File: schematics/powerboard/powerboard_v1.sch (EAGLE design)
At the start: 38 parts, among them IC1 ACS756LCB-100B-PFF-T, IC2 ATMEGA644-A, Y1 10MHZ

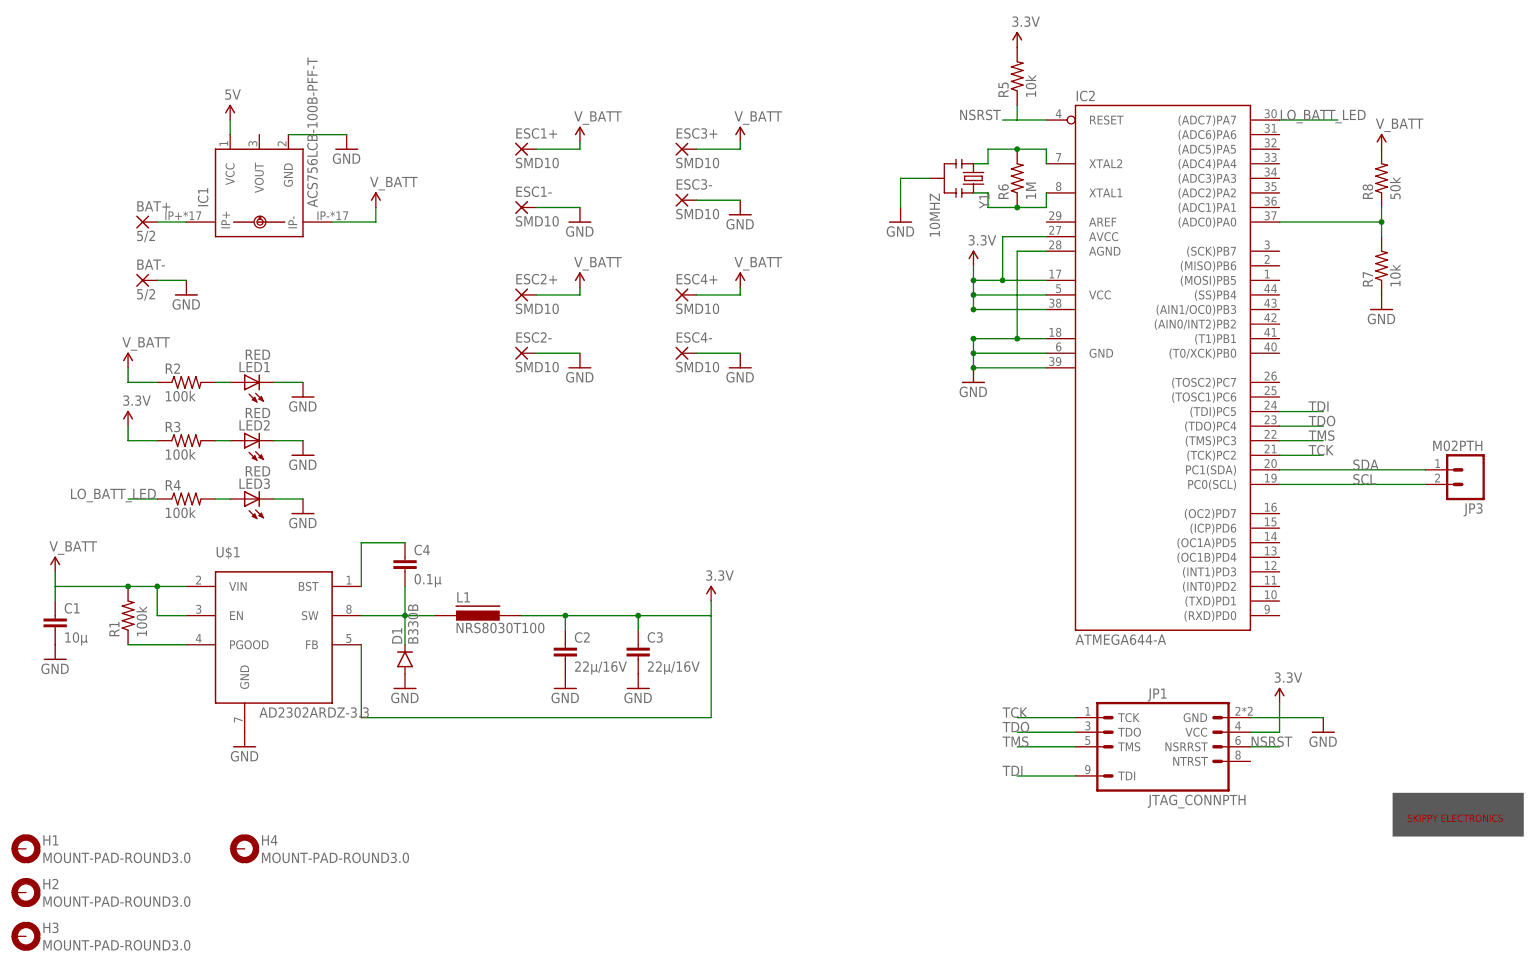
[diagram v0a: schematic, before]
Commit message: New PCB for power board
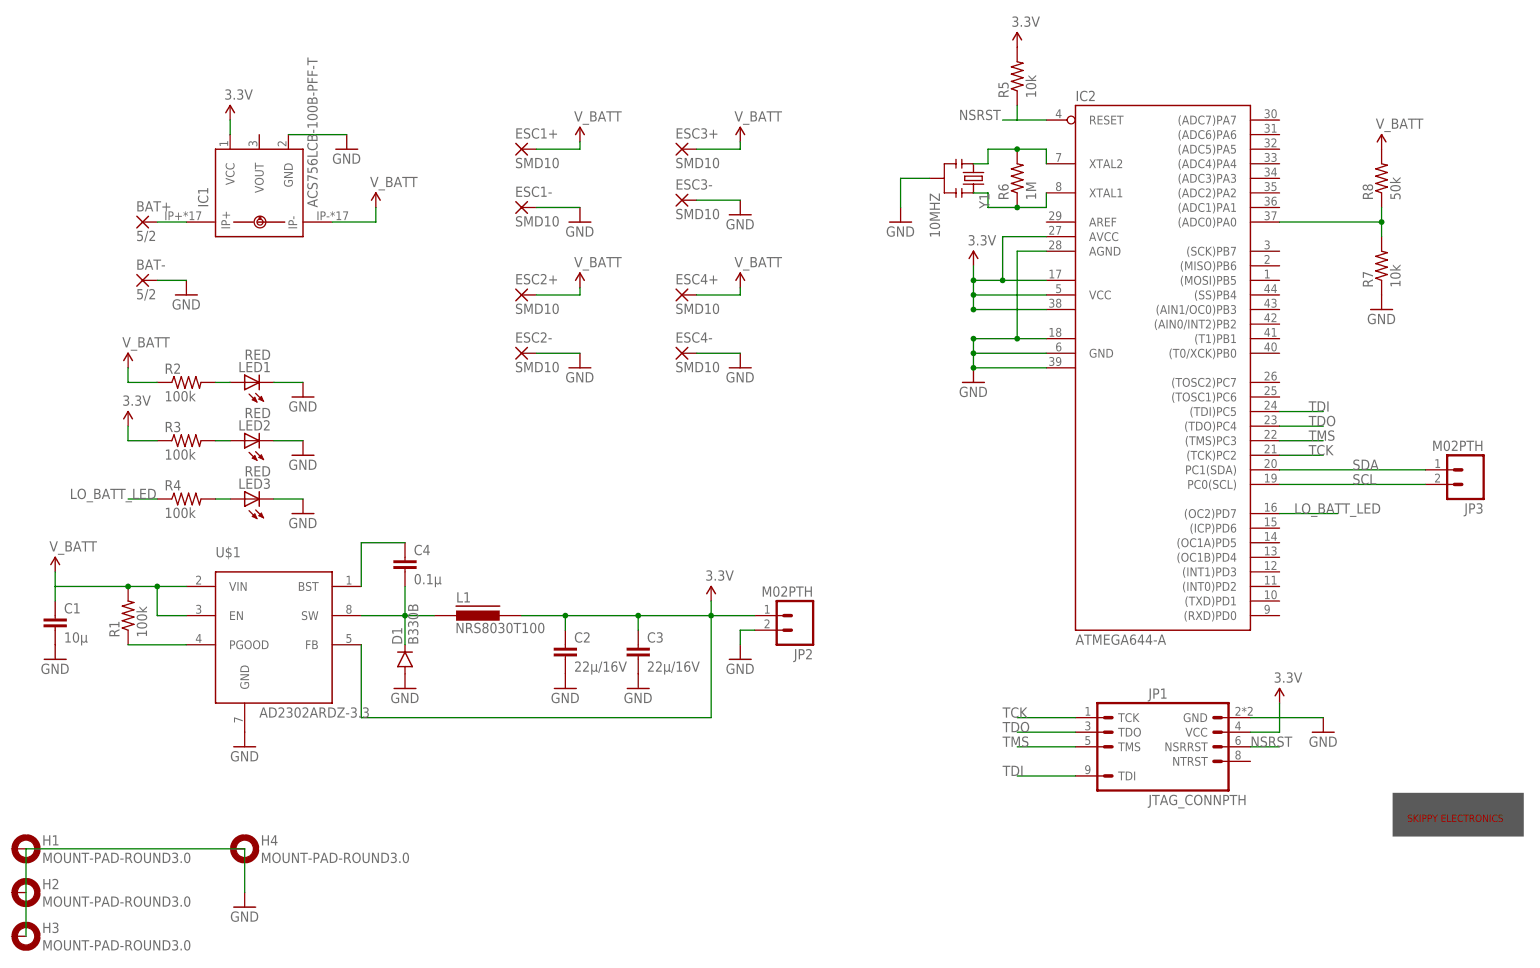
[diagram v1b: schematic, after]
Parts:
- added JP2: M02PTH, SparkFun-Connectors:M02PTH
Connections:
- removed net 5V: IC1.VCC
- net 3.3V: now also IC1.VCC, JP2.1
- net GND: now also JP2.2
- net LO_BATT_LED: now also IC2.(OC2)PD7; no longer IC2.(ADC7)PA7
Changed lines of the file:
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@@
 <?xml version="1.0" encoding="utf-8"?>
 <!DOCTYPE eagle SYSTEM "eagle.dtd">
-<eagle version="6.5.0">
+<eagle version="7.2.0">
 <drawing>
 <settings>
@@
 <part name="GND10" library="SparkFun-Aesthetics" deviceset="GND" device=""/>
 <part name="SUPPLY6" library="SparkFun-Aesthetics" deviceset="V_BATT" device=""/>
-<part name="SUPPLY8" library="SparkFun-Aesthetics" deviceset="5V" device=""/>
 <part name="GND11" library="SparkFun-Aesthetics" deviceset="GND" device=""/>
 <part name="U$1" library="dcdcconv" deviceset="AD2302ARDZ-3.3" device=""/>
@@
 <part name="H4" library="holes" deviceset="MOUNT-PAD-ROUND" device="3.0"/>
 <part name="JP3" library="SparkFun-Connectors" deviceset="M02" device="PTH"/>
+<part name="SUPPLY8" library="SparkFun-Aesthetics" deviceset="3.3V" device=""/>
+<part name="JP2" library="SparkFun-Connectors" deviceset="M02" device="PTH"/>
+<part name="GND19" library="SparkFun-Aesthetics" deviceset="GND" device=""/>
+<part name="GND20" library="SparkFun-Aesthetics" deviceset="GND" device=""/>
 </parts>
 <sheets>
@@
 <instance part="GND10" gate="1" x="15.24" y="53.34"/>
 <instance part="SUPPLY6" gate="G$1" x="15.24" y="68.58"/>
-<instance part="SUPPLY8" gate="G$1" x="45.72" y="147.32"/>
 <instance part="GND11" gate="1" x="66.04" y="142.24"/>
 <instance part="U$1" gate="G$1" x="53.34" y="58.42"/>
@@
 <instance part="H4" gate="G$1" x="48.26" y="20.32"/>
 <instance part="JP3" gate="G$1" x="261.62" y="86.36" rot="R180"/>
+<instance part="SUPPLY8" gate="G$1" x="45.72" y="147.32"/>
+<instance part="JP2" gate="G$1" x="144.78" y="60.96" rot="R180"/>
+<instance part="GND19" gate="1" x="134.62" y="53.34"/>
+<instance part="GND20" gate="1" x="48.26" y="10.16"/>
 </instances>
 <busses>
@@
 <pinref part="GND18" gate="1" pin="GND"/>
 </segment>
+<segment>
+<pinref part="JP2" gate="G$1" pin="2"/>
+<pinref part="GND19" gate="1" pin="GND"/>
+<wire x1="137.16" y1="58.42" x2="134.62" y2="58.42" width="0.1524" layer="91"/>
+<wire x1="134.62" y1="58.42" x2="134.62" y2="55.88" width="0.1524" layer="91"/>
+</segment>
+<segment>
+<wire x1="48.26" y1="20.32" x2="10.16" y2="20.32" width="0.1524" layer="91"/>
+<wire x1="10.16" y1="20.32" x2="10.16" y2="5.08" width="0.1524" layer="91"/>
+<pinref part="GND20" gate="1" pin="GND"/>
+<wire x1="48.26" y1="20.32" x2="48.26" y2="12.7" width="0.1524" layer="91"/>
+</segment>
 </net>
 <net name="N$1" class="0">
@@
 <wire x1="68.58" y1="73.66" x2="76.2" y2="73.66" width="0.1524" layer="91"/>
 <pinref part="U$1" gate="G$1" pin="BST"/>
-</segment>
-</net>
-<net name="5V" class="0">
-<segment>
-<pinref part="SUPPLY8" gate="G$1" pin="5V"/>
-<pinref part="IC1" gate="G$1" pin="VCC"/>
-<wire x1="45.72" y1="147.32" x2="45.72" y2="144.78" width="0.1524" layer="91"/>
 </segment>
 </net>
@@
 <junction x="104.14" y="60.96"/>
 <junction x="116.84" y="60.96"/>
+<pinref part="JP2" gate="G$1" pin="1"/>
+<wire x1="137.16" y1="60.96" x2="129.54" y2="60.96" width="0.1524" layer="91"/>
+<junction x="129.54" y="60.96"/>
 </segment>
 <segment>
@@
 <pinref part="SUPPLY13" gate="G$1" pin="3.3V"/>
 </segment>
+<segment>
+<pinref part="IC1" gate="G$1" pin="VCC"/>
+<wire x1="45.72" y1="147.32" x2="45.72" y2="144.78" width="0.1524" layer="91"/>
+<pinref part="SUPPLY8" gate="G$1" pin="3.3V"/>
+</segment>
 </net>
 <net name="N$4" class="0">
@@
 </segment>
 <segment>
-<pinref part="IC2" gate="G$1" pin="(ADC7)PA7"/>
-<wire x1="228.6" y1="147.32" x2="238.76" y2="147.32" width="0.1524" layer="91"/>
-<label x="228.6" y="147.32" size="1.778" layer="95"/>
-</segment>
-</net>
+<label x="231.14" y="78.74" size="1.778" layer="95"/>
+<pinref part="IC2" gate="G$1" pin="(OC2)PD7"/>
+<wire x1="228.6" y1="78.74" x2="238.76" y2="78.74" width="0.1524" layer="91"/>
+</segment>
+</net>
